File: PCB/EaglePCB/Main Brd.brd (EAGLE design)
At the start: 109.2 x 66 mm, 56 parts, among them J1 1909763-1, J3 1909763-1, U1 ATWINC1500-MR210PB1952-T, U3 MSP430FR2355TDBTRDBT0038A_M, U6 ARJM11C7-114-BA-EW2

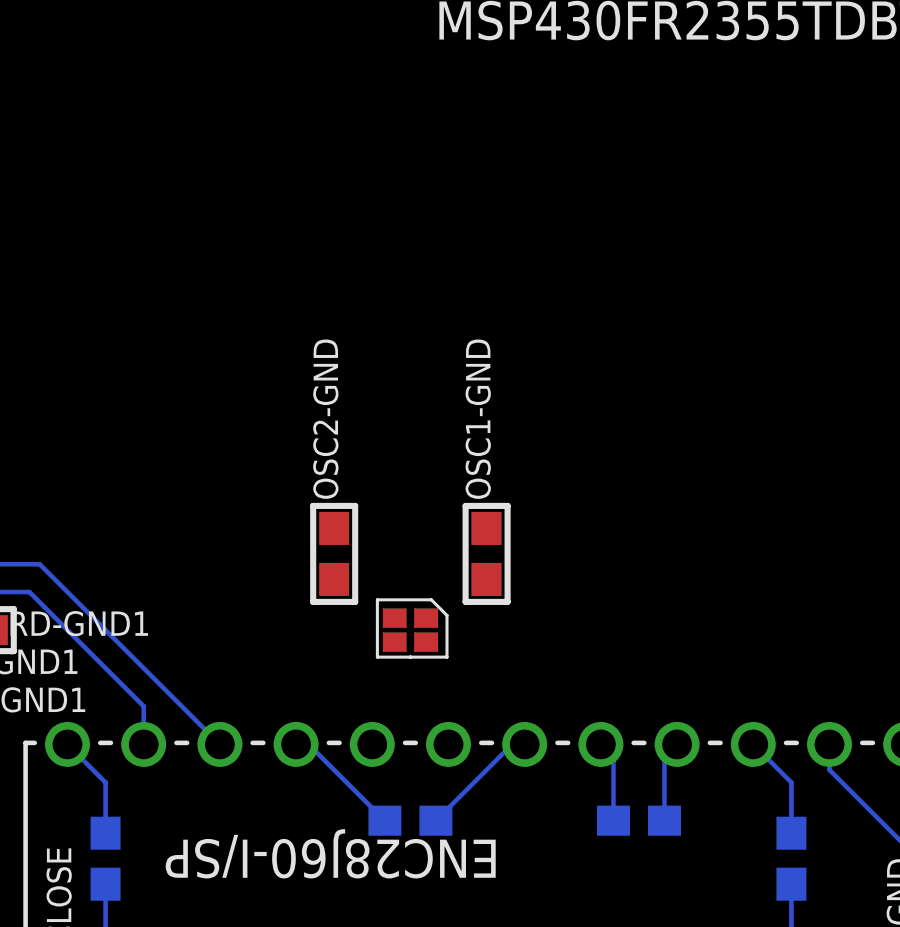
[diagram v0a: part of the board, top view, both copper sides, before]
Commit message: new oscillator added into circuit
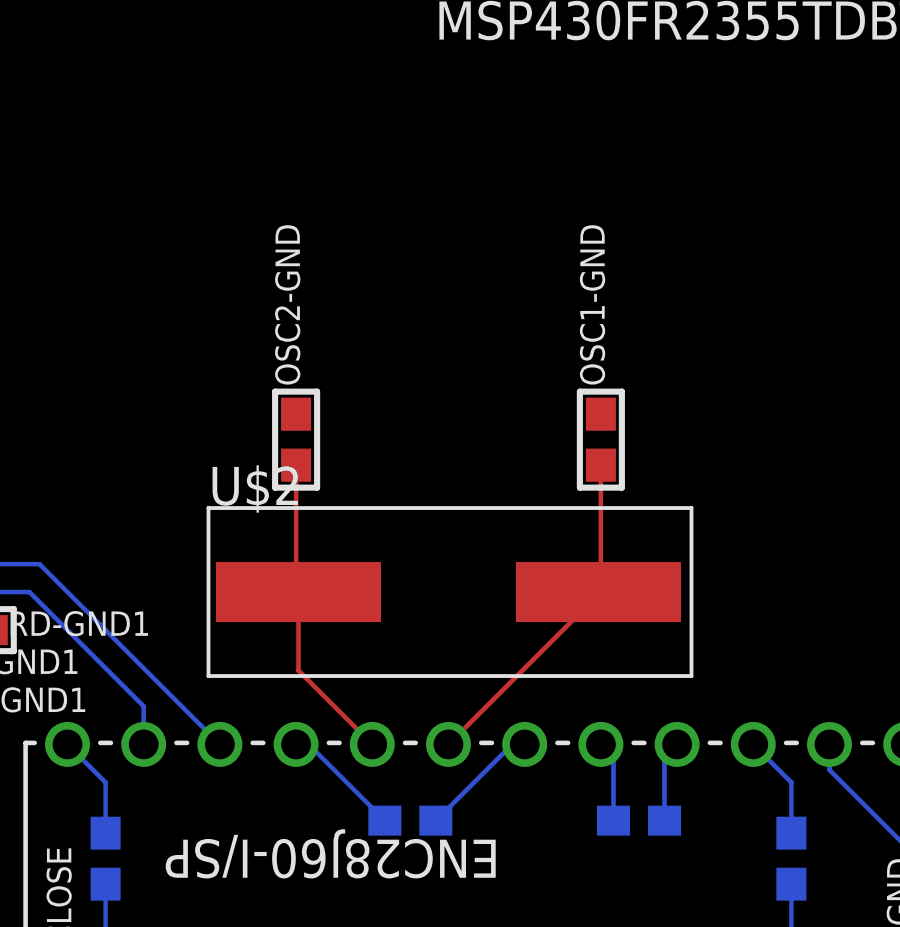
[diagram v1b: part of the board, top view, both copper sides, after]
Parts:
- U$2: value CRYSTAL -> J49SMH-P-G-G-K-25M0; device 473:4-SMD-PACKAGE -> 473:2PAD-11.5X4.8
- moved OSC1-GND 5.39 mm to (49.5, 30.5)
- moved OSC2-GND 4.02 mm to (39.4, 30.5)
- moved U$2 1.80 mm to (44.5, 25.4), turned to 0 degrees
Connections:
- net OSC1_ETH: now also U$2.P$2; no longer U$2.P$1
- net OSC2_ETH: now also U$2.P$1; no longer U$2.P$4
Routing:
- net OSC1_ETH: track 0.00 -> 11.4 mm
- net OSC2_ETH: track 0.00 -> 10.4 mm
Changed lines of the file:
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@@
 <attribute name="VALUE" x="49.022" y="17.018" size="0.4064" layer="28" font="vector" ratio="10" rot="MR0"/>
 </element>
-<element name="U$2" library="473" package="4-SMD-PACKAGE" value="CRYSTAL" x="43.18" y="24.13" smashed="yes" rot="R180"/>
-<element name="OSC2-GND" library="microbuilder" package="0603" value="180 pF" x="40.64" y="26.67" smashed="yes" rot="R90">
-<attribute name="NAME" x="40.767" y="28.448" size="0.8128" layer="25" font="vector" ratio="18" rot="R90"/>
-<attribute name="VALUE" x="41.402" y="28.448" size="0.4064" layer="27" font="vector" ratio="10" rot="R90"/>
+<element name="OSC2-GND" library="microbuilder" package="0603" value="180 pF" x="39.37" y="30.48" smashed="yes" rot="R90">
+<attribute name="NAME" x="39.497" y="32.258" size="0.8128" layer="25" font="vector" ratio="18" rot="R90"/>
+<attribute name="VALUE" x="40.132" y="32.258" size="0.4064" layer="27" font="vector" ratio="10" rot="R90"/>
 </element>
-<element name="OSC1-GND" library="microbuilder" package="0603" value="14pF" x="45.72" y="26.67" smashed="yes" rot="R90">
-<attribute name="NAME" x="45.847" y="28.448" size="0.8128" layer="25" font="vector" ratio="18" rot="R90"/>
-<attribute name="VALUE" x="46.482" y="28.448" size="0.4064" layer="27" font="vector" ratio="10" rot="R90"/>
+<element name="OSC1-GND" library="microbuilder" package="0603" value="14pF" x="49.53" y="30.48" smashed="yes" rot="R90">
+<attribute name="NAME" x="49.657" y="32.258" size="0.8128" layer="25" font="vector" ratio="18" rot="R90"/>
+<attribute name="VALUE" x="50.292" y="32.258" size="0.4064" layer="27" font="vector" ratio="10" rot="R90"/>
+</element>
+<element name="U$2" library="473" package="2PAD-11.5X4.8" value="J49SMH-P-G-G-K-25M0" x="44.45" y="25.4" smashed="yes">
+<attribute name="NAME" x="36.45" y="28.3" size="1.27" layer="25"/>
+<attribute name="VALUE" x="36.35" y="21.2" size="1.27" layer="27"/>
 </element>
 </elements>
@@
 <wire x1="64.77" y1="9.365" x2="86.98" y2="8.0264" width="0" layer="19" extent="1-1"/>
 <wire x1="60.96" y1="6.35" x2="64.77" y2="9.365" width="0" layer="19" extent="1-1"/>
-<wire x1="45.72" y1="27.52" x2="64.77" y2="9.365" width="0" layer="19" extent="1-1"/>
-<wire x1="40.64" y1="27.52" x2="45.72" y2="27.52" width="0" layer="19" extent="1-1"/>
-<wire x1="29.21" y1="24.13" x2="40.64" y2="27.52" width="0" layer="19" extent="1-1"/>
+<wire x1="49.53" y1="31.33" x2="64.77" y2="9.365" width="0" layer="19" extent="1-1"/>
+<wire x1="39.37" y1="31.33" x2="49.53" y2="31.33" width="0" layer="19" extent="1-1"/>
+<wire x1="29.21" y1="24.13" x2="39.37" y2="31.33" width="0" layer="19" extent="1-1"/>
 <wire x1="27.32" y1="17.78" x2="29.21" y2="24.13" width="0" layer="19" extent="1-1"/>
 <wire x1="20.32" y1="12.7" x2="27.32" y2="17.78" width="0" layer="19" extent="1-1"/>
@@
 <signal name="OSC1_ETH">
 <contactref element="ETH" pad="23"/>
-<contactref element="U$2" pad="P$1"/>
 <contactref element="OSC1-GND" pad="1"/>
-<wire x1="43.71" y1="24.53" x2="45.72" y2="25.82" width="0" layer="19" extent="1-1"/>
-<wire x1="44.45" y1="20.32" x2="43.71" y2="24.53" width="0" layer="19" extent="1-1"/>
+<contactref element="U$2" pad="P$2"/>
+<wire x1="49.45" y1="25.4" x2="49.45" y2="25.32" width="0.1524" layer="1"/>
+<wire x1="49.45" y1="25.32" x2="44.45" y2="20.32" width="0.1524" layer="1"/>
+<wire x1="49.45" y1="25.4" x2="49.53" y2="25.48" width="0.1524" layer="1"/>
+<wire x1="49.53" y1="25.48" x2="49.53" y2="29.63" width="0.1524" layer="1"/>
 </signal>
 <signal name="OSC2_ETH">
 <contactref element="ETH" pad="24"/>
-<contactref element="U$2" pad="P$4"/>
 <contactref element="OSC2-GND" pad="1"/>
-<wire x1="42.65" y1="23.73" x2="40.64" y2="25.82" width="0" layer="19" extent="1-1"/>
-<wire x1="41.91" y1="20.32" x2="42.65" y2="23.73" width="0" layer="19" extent="1-1"/>
+<contactref element="U$2" pad="P$1"/>
+<wire x1="39.37" y1="29.63" x2="39.37" y2="25.48" width="0.1524" layer="1"/>
+<wire x1="39.45" y1="25.4" x2="39.37" y2="25.48" width="0.1524" layer="1"/>
+<wire x1="39.45" y1="25.4" x2="39.45" y2="22.78" width="0.1524" layer="1"/>
+<wire x1="39.45" y1="22.78" x2="41.91" y2="20.32" width="0.1524" layer="1"/>
 </signal>
 </signals>

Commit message: routed TDP TDM Crystal
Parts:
- moved RD-GND1 10.9 mm to (19.5, 30.5)
- moved TCT-3V3 8.03 mm to (17.8, 27.9), turned to 180 degrees
- moved RDM-GND1 1.27 mm to (25.4, 20.3)
- flipped OSC1-GND to the bottom
- flipped OSC2-GND to the bottom
- turned RFI-GND1 to 180 degrees
- flipped U$2 to the bottom, turned to 180 degrees
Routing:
- net TDM: track 0.00 -> 43.5 mm
- net TDP: track 0.00 -> 41.0 mm, vias 0 -> 1
- net TDC: track 12.7 -> 24.2 mm
- net VR_PA: track 0.00 -> 8.98 mm
- net VR_PA2: track 0.00 -> 8.98 mm
- net RFO: track 0.00 -> 8.05 mm
- net RFO2: track 0.00 -> 8.05 mm
- net PA_BOOST: track 0.00 -> 5.00 mm
- net PA_BOOST2: track 0.00 -> 5.00 mm
- net ANT3-2: track 0.00 -> 4.52 mm
- net ANT3: track 0.00 -> 4.52 mm
- net ANT1: track 0.00 -> 4.05 mm
- net ANT1-2: track 0.00 -> 4.05 mm
- net RFI: track 0.00 -> 3.66 mm
- net RFI2: track 0.00 -> 3.66 mm
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
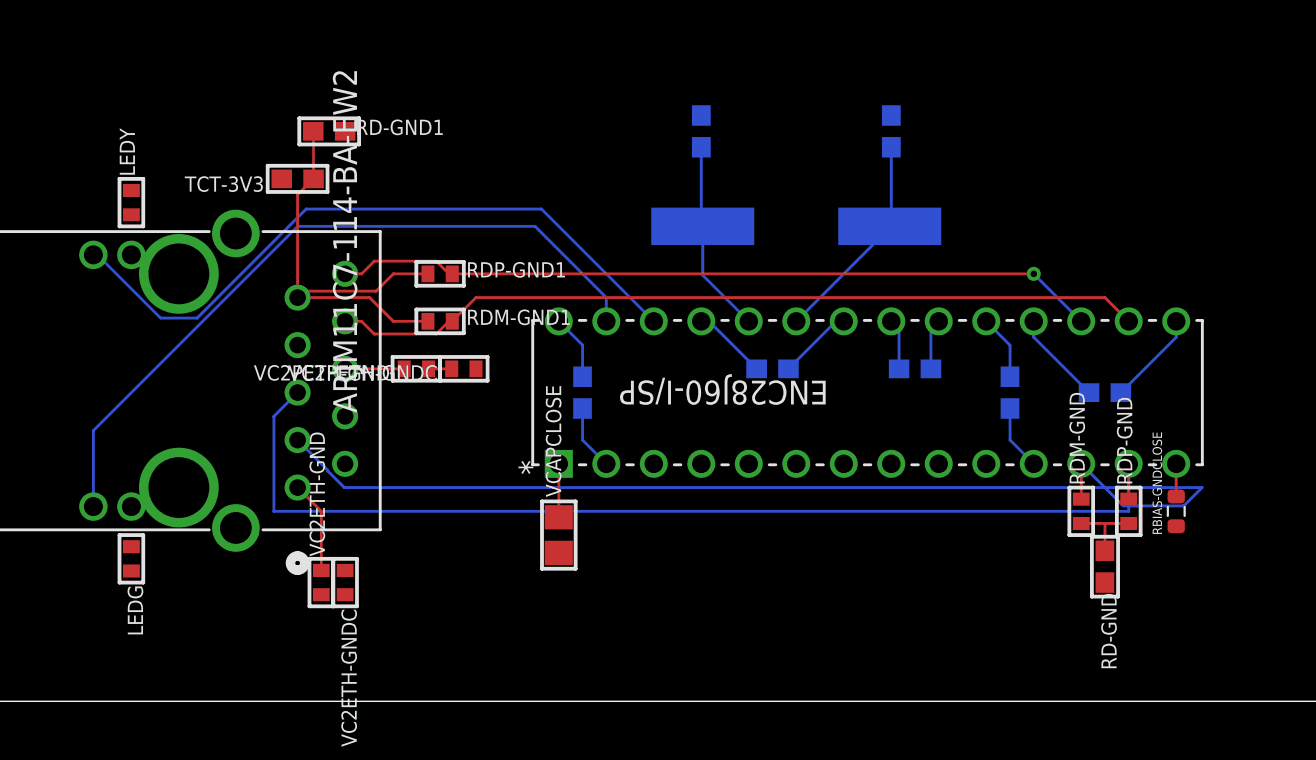
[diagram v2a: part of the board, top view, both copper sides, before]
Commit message: moved 3V3
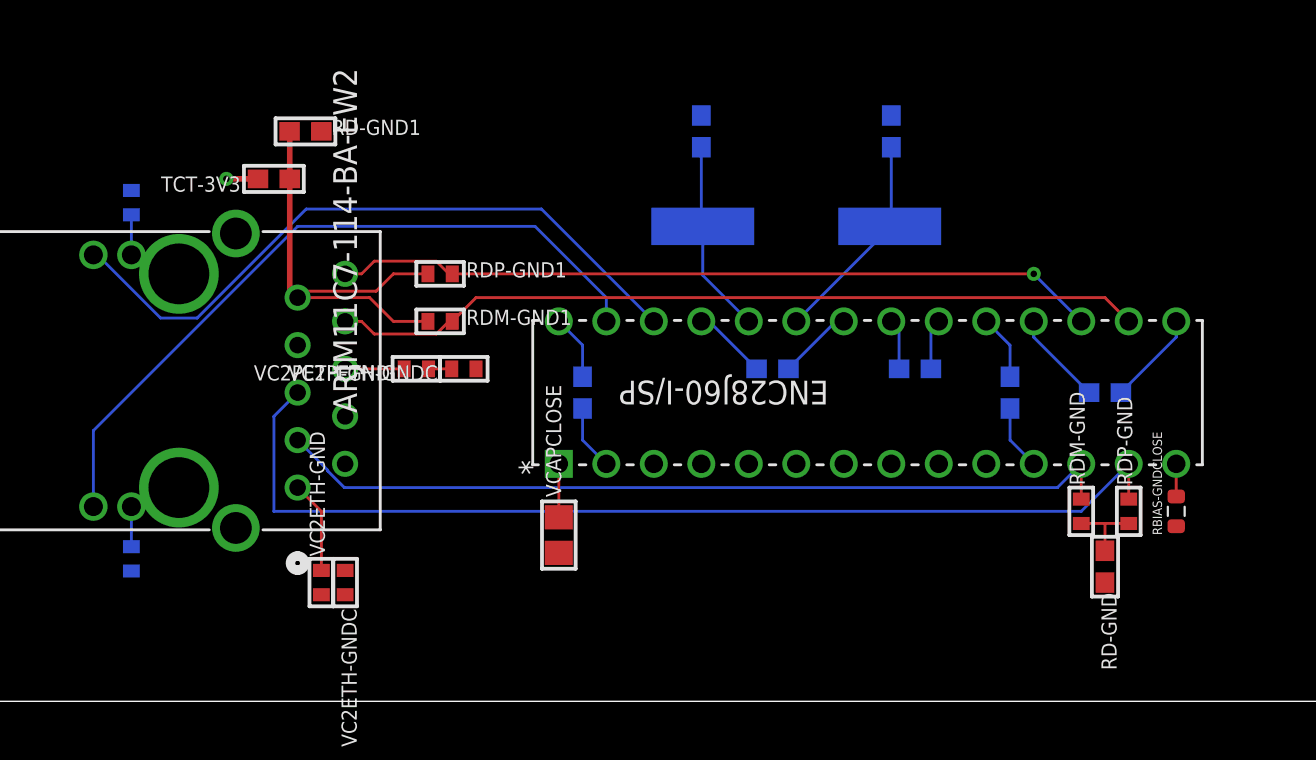
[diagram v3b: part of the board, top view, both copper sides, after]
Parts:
- moved RD-GND1 1.27 mm to (18.2, 30.5)
- moved TCT-3V3 1.27 mm to (16.5, 27.9)
- flipped LEDG to the bottom
- flipped LEDY to the bottom
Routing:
- net RDM: track 59.1 -> 45.4 mm
- net N$9: track 0.00 -> 2.14 mm
- net N$7: track 0.00 -> 2.14 mm
- net 3V3: track 0.00 -> 1.69 mm, vias 0 -> 1
- net RDP: track 57.0 -> 55.5 mm
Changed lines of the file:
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@@
 <attribute name="VALUE" x="26.797" y="22.225" size="0.4064" layer="27" ratio="10"/>
 </element>
-<element name="RD-GND1" library="microbuilder" package="0603" value="0.1 uF" x="19.47" y="30.48" smashed="yes">
-<attribute name="NAME" x="20.867" y="30.2895" size="0.8128" layer="25" ratio="18"/>
-<attribute name="VALUE" x="20.867" y="29.845" size="0.4064" layer="27" ratio="10"/>
-</element>
-<element name="TCT-3V3" library="microbuilder" package="0603" value="" x="17.78" y="27.94" smashed="yes" rot="R180">
-<attribute name="NAME" x="16.002" y="28.067" size="0.8128" layer="25" font="vector" ratio="18" rot="R180"/>
-<attribute name="VALUE" x="16.002" y="28.702" size="0.4064" layer="27" font="vector" ratio="10" rot="R180"/>
+<element name="RD-GND1" library="microbuilder" package="0603" value="0.1 uF" x="18.2" y="30.48" smashed="yes">
+<attribute name="NAME" x="19.597" y="30.2895" size="0.8128" layer="25" ratio="18"/>
+<attribute name="VALUE" x="19.597" y="29.845" size="0.4064" layer="27" ratio="10"/>
+</element>
+<element name="TCT-3V3" library="microbuilder" package="0603" value="" x="16.51" y="27.94" smashed="yes" rot="R180">
+<attribute name="NAME" x="14.732" y="28.067" size="0.8128" layer="25" font="vector" ratio="18" rot="R180"/>
+<attribute name="VALUE" x="14.732" y="28.702" size="0.4064" layer="27" font="vector" ratio="10" rot="R180"/>
 </element>
 <element name="VCAPCLOSE" library="microbuilder" package="0805" value="10 uF" x="31.75" y="8.89" smashed="yes" rot="R90">
@@
 <attribute name="VALUE" x="32.512" y="10.922" size="0.4064" layer="27" ratio="10" rot="R90"/>
 </element>
-<element name="LEDG" library="microbuilder" package="0402" value="" x="8.89" y="7.62" smashed="yes" rot="R270">
-<attribute name="NAME" x="8.6995" y="6.223" size="0.8128" layer="25" ratio="18" rot="R270"/>
-<attribute name="VALUE" x="8.255" y="6.223" size="0.4064" layer="27" ratio="10" rot="R270"/>
-</element>
-<element name="LEDY" library="microbuilder" package="0402" value="" x="8.89" y="26.67" smashed="yes" rot="R90">
-<attribute name="NAME" x="9.0805" y="28.067" size="0.8128" layer="25" ratio="18" rot="R90"/>
-<attribute name="VALUE" x="9.525" y="28.067" size="0.4064" layer="27" ratio="10" rot="R90"/>
+<element name="LEDG" library="microbuilder" package="0402" value="" x="8.89" y="7.62" smashed="yes" rot="MR270">
+<attribute name="NAME" x="9.0805" y="6.223" size="0.8128" layer="26" ratio="18" rot="MR270"/>
+<attribute name="VALUE" x="9.525" y="6.223" size="0.4064" layer="28" ratio="10" rot="MR270"/>
+</element>
+<element name="LEDY" library="microbuilder" package="0402" value="" x="8.89" y="26.67" smashed="yes" rot="MR90">
+<attribute name="NAME" x="8.6995" y="28.067" size="0.8128" layer="26" ratio="18" rot="MR90"/>
+<attribute name="VALUE" x="8.255" y="28.067" size="0.4064" layer="28" ratio="10" rot="MR90"/>
 </element>
 <element name="RBIAS-GNDCLOSE" library="Resistor_Capacitor" library_urn="urn:adsk.eagle:library:15122775" package="RES_0603" package3d_urn="urn:adsk.eagle:package:10872900/3" value="2.32K 1%" x="64.77" y="10.16" smashed="yes" rot="R90">
@@
 <wire x1="49.53" y1="31.33" x2="64.77" y2="9.365" width="0" layer="19" extent="1-1"/>
 <wire x1="39.37" y1="31.33" x2="49.53" y2="31.33" width="0" layer="19" extent="1-1"/>
-<wire x1="20.32" y1="30.48" x2="39.37" y2="31.33" width="0" layer="19" extent="1-1"/>
-<wire x1="27.32" y1="17.78" x2="20.32" y2="30.48" width="0" layer="19" extent="1-1"/>
+<wire x1="19.05" y1="30.48" x2="39.37" y2="31.33" width="0" layer="19" extent="1-1"/>
+<wire x1="27.32" y1="17.78" x2="19.05" y2="30.48" width="0" layer="19" extent="1-1"/>
 <wire x1="20.32" y1="12.7" x2="27.32" y2="17.78" width="0" layer="19" extent="1-1"/>
 <wire x1="20.32" y1="7" x2="20.32" y2="12.7" width="0" layer="19" extent="1-1"/>
@@
 <contactref element="ETH" pad="13"/>
 <wire x1="62.23" y1="10.81" x2="62.23" y2="12.7" width="0.1524" layer="1"/>
-<wire x1="16.51" y1="10.16" x2="16.51" y2="15.24" width="0.1524" layer="16"/>
-<wire x1="62.23" y1="12.7" x2="62.23" y2="10.16" width="0.1524" layer="16"/>
-<wire x1="62.23" y1="10.16" x2="16.51" y2="10.16" width="0.1524" layer="16"/>
+<wire x1="16.51" y1="15.24" x2="16.51" y2="10.16" width="0.1524" layer="16"/>
 <wire x1="16.51" y1="15.24" x2="17.78" y2="16.51" width="0.1524" layer="16"/>
+<wire x1="16.51" y1="10.16" x2="59.69" y2="10.16" width="0.1524" layer="16"/>
+<wire x1="59.69" y1="10.16" x2="62.23" y2="12.7" width="0.1524" layer="16"/>
 </signal>
 <signal name="RDM">
@@
 <wire x1="19.3929" y1="12.31598125" x2="19.3929" y2="12.3571" width="0.1524" layer="16"/>
 <wire x1="19.3929" y1="12.3571" x2="17.78" y2="13.97" width="0.1524" layer="16"/>
-<wire x1="59.69" y1="12.7" x2="61.93791875" y2="10.45208125" width="0.1524" layer="16"/>
-<wire x1="65.1750625" y1="10.4521" x2="61.93791875" y2="10.45208125" width="0.1524" layer="16"/>
-<wire x1="66.1529625" y1="11.43" x2="65.1750625" y2="10.4521" width="0.1524" layer="16"/>
-<wire x1="66.1529625" y1="11.43" x2="20.27888125" y2="11.43" width="0.1524" layer="16"/>
-<wire x1="20.27888125" y1="11.43" x2="19.3929" y2="12.31598125" width="0.1524" layer="16"/>
+<wire x1="19.3929" y1="12.31598125" x2="20.27888125" y2="11.43" width="0.1524" layer="16"/>
+<wire x1="20.27888125" y1="11.43" x2="58.42" y2="11.43" width="0.1524" layer="16"/>
+<wire x1="58.42" y1="11.43" x2="59.69" y2="12.7" width="0.1524" layer="16"/>
 </signal>
 <signal name="N$8">
@@
 <contactref element="RD-GND1" pad="1"/>
 <contactref element="TCT-3V3" pad="1"/>
-<wire x1="18.63" y1="27.94" x2="17.78" y2="27.09" width="0.1524" layer="1"/>
-<wire x1="17.78" y1="27.09" x2="17.78" y2="21.59" width="0.1524" layer="1"/>
-<wire x1="18.63" y1="27.94" x2="18.63" y2="30.47" width="0.1524" layer="1"/>
-<wire x1="18.63" y1="30.47" x2="18.62" y2="30.48" width="0.1524" layer="1"/>
 <wire x1="24.75" y1="22.86" x2="22.90111875" y2="22.86" width="0.1524" layer="1"/>
 <wire x1="18.1229" y1="21.9329" x2="17.78" y2="21.59" width="0.1524" layer="1"/>
@@
 <wire x1="22.90111875" y1="20.32" x2="21.63111875" y2="21.59" width="0.1524" layer="1"/>
 <wire x1="21.63111875" y1="21.59" x2="17.78" y2="21.59" width="0.1524" layer="1"/>
+<wire x1="17.35" y1="30.48" x2="17.36" y2="30.47" width="0.3048" layer="1"/>
+<wire x1="17.36" y1="30.47" x2="17.36" y2="27.94" width="0.3048" layer="1"/>
+<wire x1="17.36" y1="27.94" x2="17.36" y2="22.01" width="0.3048" layer="1"/>
+<wire x1="17.78" y1="21.59" x2="17.36" y2="22.01" width="0.3048" layer="1"/>
 </signal>
 <signal name="3V3">
@@
 <contactref element="LEDY" pad="2"/>
 <contactref element="LEDG" pad="2"/>
-<wire x1="8.89" y1="6.97" x2="8.89" y2="27.32" width="0" layer="19" extent="1-1"/>
-<wire x1="16.93" y1="27.94" x2="8.89" y2="6.97" width="0" layer="19" extent="1-1"/>
+<wire x1="15.66" y1="27.94" x2="13.97" y2="27.94" width="0.3048" layer="1"/>
+<via x="13.97" y="27.94" extent="1-16" drill="0.35"/>
+<wire x1="8.89" y1="27.32" x2="13.97" y2="27.94" width="0" layer="19" extent="16-16"/>
+<wire x1="8.89" y1="6.97" x2="8.89" y2="27.32" width="0" layer="19" extent="16-16"/>
 </signal>
 <signal name="N$4">
@@
 <contactref element="LEDY" pad="1"/>
 <contactref element="U6" pad="13"/>
-<wire x1="8.89" y1="26.02" x2="8.89" y2="23.876" width="0" layer="19" extent="1-1"/>
+<wire x1="8.89" y1="23.876" x2="8.89" y2="26.02" width="0.1524" layer="16"/>
 </signal>
 <signal name="N$9">
 <contactref element="U6" pad="11"/>
 <contactref element="LEDG" pad="1"/>
-<wire x1="8.89" y1="10.414" x2="8.89" y2="8.27" width="0" layer="19" extent="1-1"/>
+<wire x1="8.89" y1="10.414" x2="8.89" y2="8.27" width="0.1524" layer="16"/>
 </signal>
 <signal name="N$10">
